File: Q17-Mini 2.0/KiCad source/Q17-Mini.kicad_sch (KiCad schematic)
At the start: 83 parts, among them J1 INPUT, J2-1 SPK+, J2-2 SPK-, J3-1 V+, J3-2 GND, J3-3 V-, Q1 IRF610, Q10 KSA992, Q12 KSC1845, Q13 IRF610, Q14 IRF9610, Q15 FQA46N15, Q16 IXTH48P20P, Q2 KSA992, Q3 KSC1845, Q4 IRF9610, Q5 FQPF7P20, Q6 2SK3564, Q7 LSK170B, Q8 DN2540, Q9 BS250P, U1 OPA1611, U2 NDC7003P

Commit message: Update BOM for Q17-Mini 2.0
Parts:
- R4: Mouser 594-MRS25000C1009FRP -> 594-MRS25000C1001FRP; Part# MRS25000C1009FRP00 -> MRS25000C1001FRP00
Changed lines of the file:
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@@
   (title_block
     (title "Q17-Mini Amplifier")
-    (date "2023-09-02")
+    (date "2023-09-14")
     (rev "2.0")
     (company "by eng. Tiberiu Vicol")
@@
       (effects (font (size 1.27 1.27)) hide)
     )
-    (property "Part#" "MRS25000C1009FRP00" (at 133.35 83.82 0)
-      (effects (font (size 1.27 1.27)) hide)
-    )
-    (property "Mouser" "594-MRS25000C1009FRP" (at 133.35 83.82 0)
-      (effects (font (size 1.27 1.27)) hide)
-    )
+    (property "Part#" "MRS25000C1001FRP00" (at 133.35 83.82 0)
+      (effects (font (size 1.27 1.27)) hide)
+    )
+    (property "Mouser" "594-MRS25000C1001FRP" (at 133.35 83.82 0)
+      (effects (font (size 1.27 1.27)) hide)
+    )

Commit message: Update schematic
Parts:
- R32: value STRAP -> 10R or STRAP; Mouser N.A -> 594-MRS25000C1009FRP; Part# N.A -> MRS25000C1009FRP00
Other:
- note added: "DC Offset at output < 1mV"
- note added: "DC Offset at output with R32 = 10R < 40mV"
- note added: "The value of R25 depends on the input voltage (42v = 2K7, 50v = 7K5, 60v = 8k2)."
- note removed: "DC Offset at output > 1mV"
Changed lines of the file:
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@@
   (title_block
     (title "Q17-Mini Amplifier")
-    (date "2023-09-14")
-    (rev "2.0")
+    (date "2023-09-24")
+    (rev "2.0.2")
     (company "by eng. Tiberiu Vicol")
     (comment 1 "Modified by Stef for the Q17-Mini project")
@@
   )
   (text "This will give you a coil of 10x20mm (see picture on github repository)."
-    (at 13.97 158.75 0)
+    (at 13.97 160.02 0)
     (effects (font (size 1.27 1.27) (thickness 0.254) bold) (justify left bottom))
   )
-  (text "For input sensibility at 1.5v: R17 = 7.32k" (at 177.8 160.02 0)
+  (text "For input sensibility at 1.5v: R17 = 7.32k" (at 177.8 157.48 0)
+    (effects (font (size 1.27 1.27)) (justify left bottom))
+  )
+  (text "The value of R25 depends on the input voltage (42v = 2K7, 50v = 7K5, 60v = 8k2)."
+    (at 177.8 162.56 0)
     (effects (font (size 1.27 1.27)) (justify left bottom))
   )
@@
   )
   (text "L1 : 19.5 turns of a 1mm diameter copper insulated wire wound around a 8mm tube."
-    (at 13.97 156.21 0)
+    (at 13.97 157.48 0)
     (effects (font (size 1.27 1.27) (thickness 0.254) bold) (justify left bottom))
   )
@@
     (effects (font (size 1.27 1.27)) (justify left bottom))
   )
-  (text "Transformer for 2 boards: 2 x 36Vac 160-250VA" (at 177.8 154.94 0)
+  (text "Transformer for 2 boards: 2 x 36Vac 160-250VA" (at 13.97 153.67 0)
     (effects (font (size 1.27 1.27) (thickness 0.254) bold) (justify left bottom))
   )
@@
     (effects (font (size 1.27 1.27)) (justify left bottom))
   )
-  (text "For input sensibility at 0.750v: R17 = 3.3k" (at 177.8 162.56 0)
+  (text "For input sensibility at 0.750v: R17 = 3.3k" (at 177.8 160.02 0)
     (effects (font (size 1.27 1.27)) (justify left bottom))
   )
@@
     (effects (font (size 1.27 1.27)) (justify left bottom))
   )
+  (text "DC Offset at output with R32 = 10R < 40mV" (at 13.97 30.48 0)
+    (effects (font (size 1.27 1.27)) (justify left bottom))
+  )
   (text "C17 : 100nF capacitor FKP3C031004C00JSSD or MKT1822410255."
     (at 107.95 189.23 0)
@@
     (effects (font (size 1.27 1.27)) (justify left bottom))
   )
-  (text "DC Offset at output > 1mV" (at 13.97 27.94 0)
+  (text "DC Offset at output < 1mV" (at 13.97 27.94 0)
     (effects (font (size 1.27 1.27)) (justify left bottom))
   )
@@
       (effects (font (size 1.27 1.27)) (justify left))
     )
-    (property "Value" "STRAP" (at 270.9647 146.2422 90)
+    (property "Value" "10R or STRAP" (at 274.32 146.05 90)
       (effects (font (size 1.27 1.27)) (justify left))
     )
@@
       (effects (font (size 1.27 1.27)) hide)
     )
-    (property "Datasheet" "~" (at 267.97 148.59 0)
+    (property "Datasheet" "https://www.vishay.com/doc?28724" (at 267.97 148.59 0)
       (effects (font (size 1.27 1.27)) hide)
     )
-    (property "Part#" "N.A" (at 267.97 148.59 90)
+    (property "Part#" "MRS25000C1009FRP00" (at 267.97 148.59 90)
       (effects (font (size 1.27 1.27)) hide)
     )
-    (property "Mouser" "N.A" (at 267.97 148.59 90)
+    (property "Mouser" "594-MRS25000C1009FRP" (at 267.97 148.59 90)
       (effects (font (size 1.27 1.27)) hide)
     )

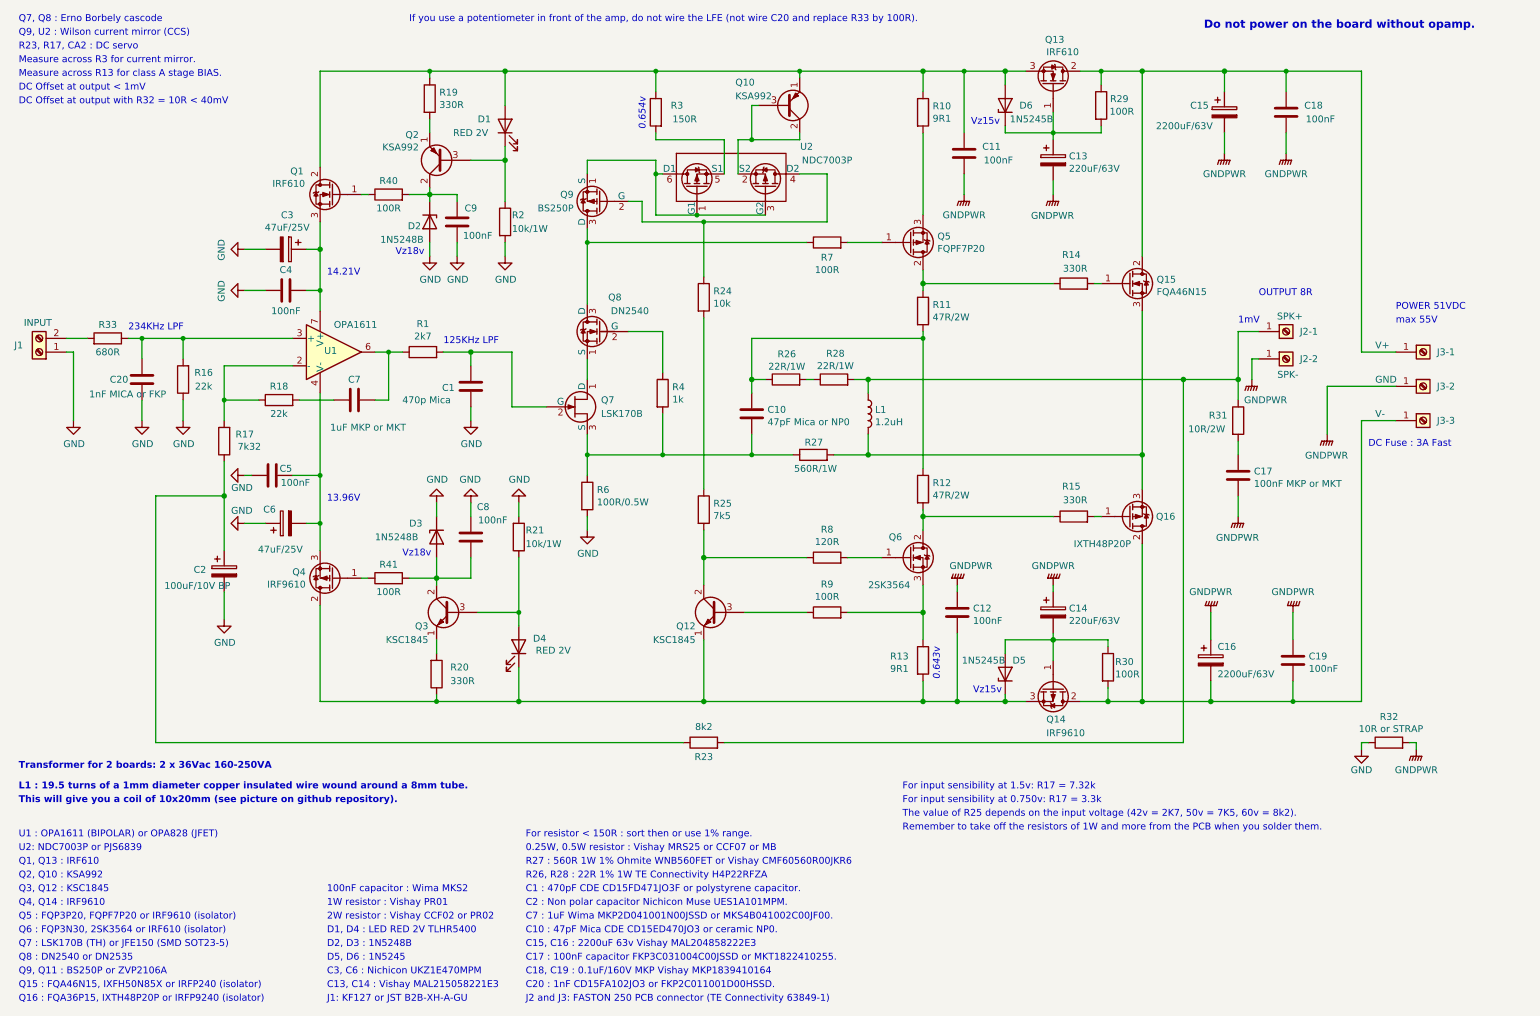
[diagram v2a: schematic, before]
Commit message: Q17-Mini-schematic 2.0.3 with measures
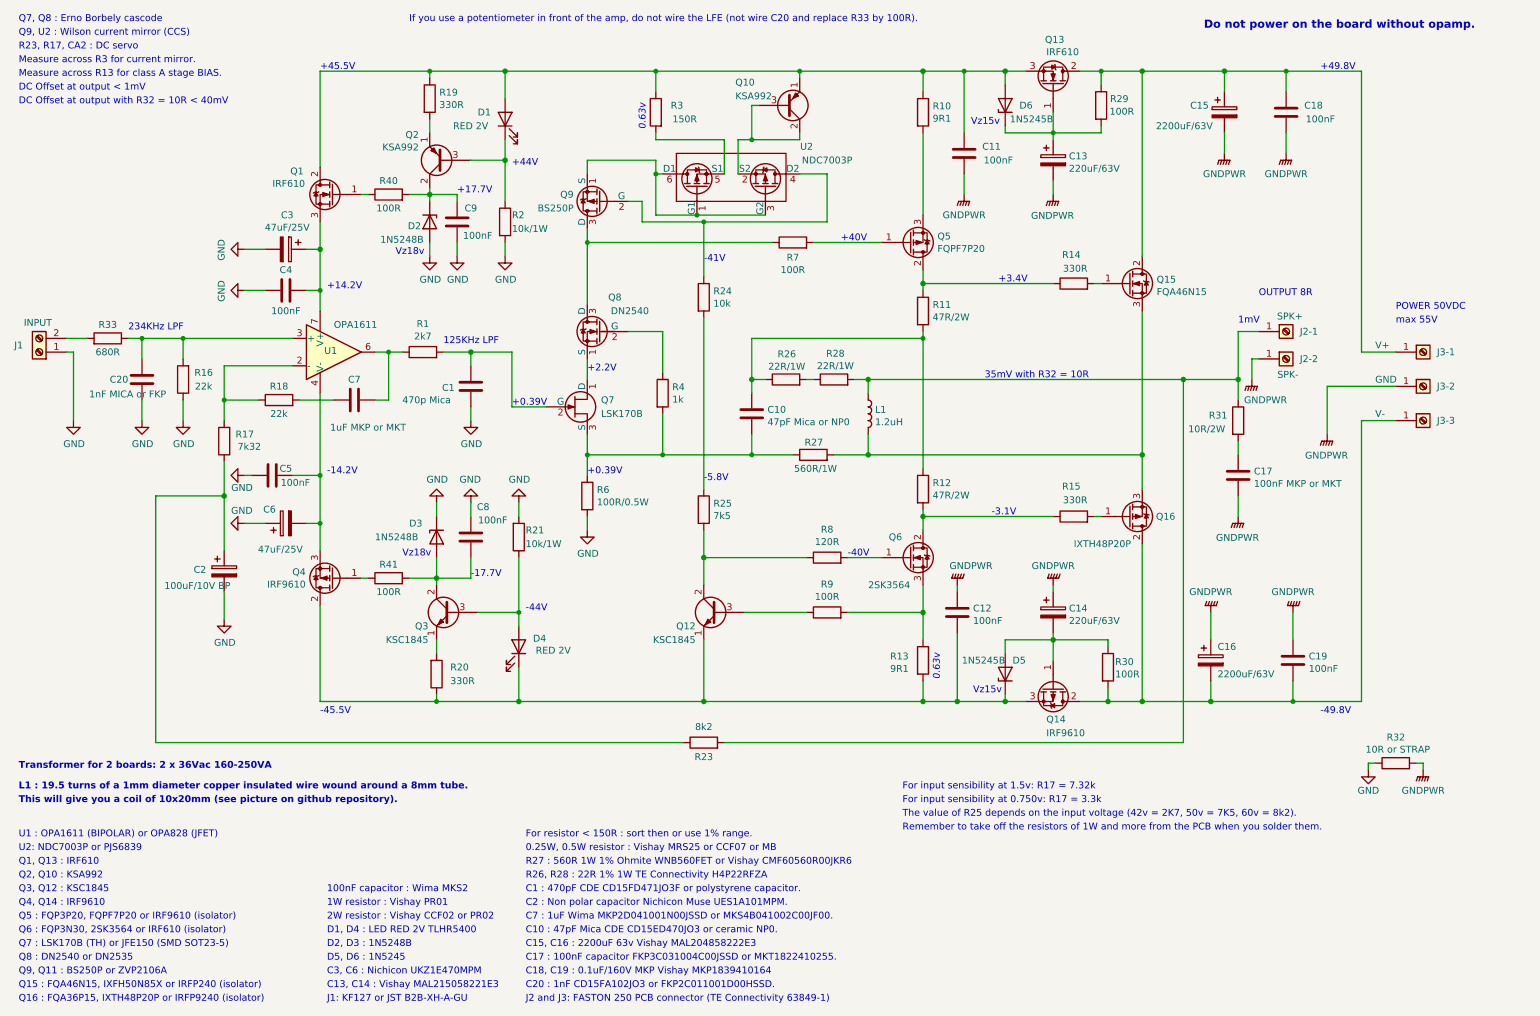
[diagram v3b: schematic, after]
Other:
- note added: "+0.39V"
- note added: "+14.2V"
- note added: "+17.7V"
- note added: "+2.2V"
- note added: "+3.4V"
- note added: "+40V"
- note added: "+44V"
- note added: "+45.5V"
- note added: "+49.8V"
- note added: "-14.2V"
- note added: "-17.7V"
- note added: "-3.1V"
- note added: "-40V"
- note added: "-41V"
- note added: "-44V"
- note added: "-45.5V"
- note added: "-49.8V"
- note added: "-5.8V"
- note added: "0.63v"
- note added: "35mV with R32 = 10R"
- note added: "POWER 50VDC"
- note removed: "0.643v"
- note removed: "0.654v"
- note removed: "13.96V"
- note removed: "14.21V"
- note removed: "DC Fuse : 3A Fast"
- note removed: "POWER 51VDC"
- title: Q17-Mini Amplifier -> Q17-Mini Amplifier 2.x
- moved on the sheet: D1, R32, R7

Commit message: Update Q17-Mini-schematic 2.0.4
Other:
- note added: "Transformer for 2 boards: 2 x 37Vac 160-250VA"
- note removed: "Transformer for 2 boards: 2 x 36Vac 160-250VA"
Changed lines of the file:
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@@
   (title_block
     (title "Q17-Mini Amplifier 2.x")
-    (date "2024-01-06")
-    (rev "2.0.3")
+    (date "2024-01-11")
+    (rev "2.0.4")
     (company "by eng. Tiberiu Vicol")
     (comment 1 "Modified by Stef for the Q17-Mini project")
@@
     (effects (font (size 1.27 1.27)) (justify left bottom))
   )
-  (text "Transformer for 2 boards: 2 x 36Vac 160-250VA" (at 13.97 153.67 0)
+  (text "Transformer for 2 boards: 2 x 37Vac 160-250VA" (at 13.97 153.67 0)
     (effects (font (size 1.27 1.27) (thickness 0.254) bold) (justify left bottom))
   )

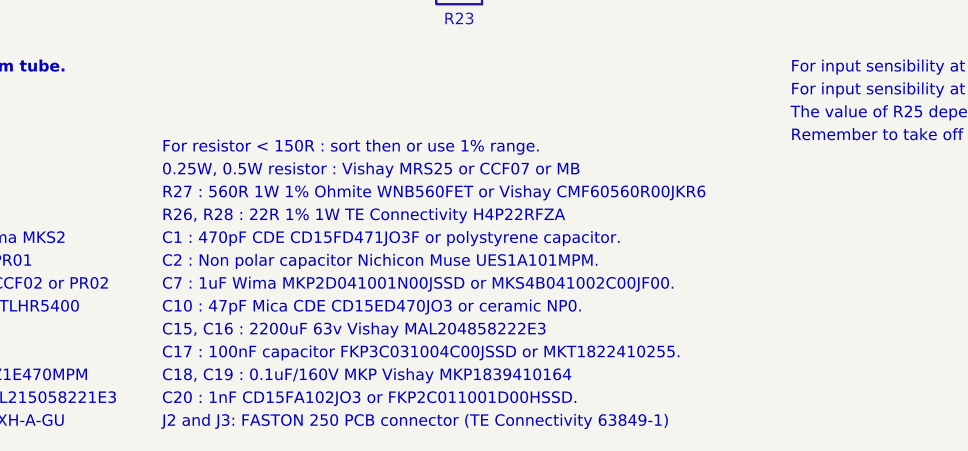
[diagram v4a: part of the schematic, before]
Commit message: Update Q17-Mini diagram (C7 parts)
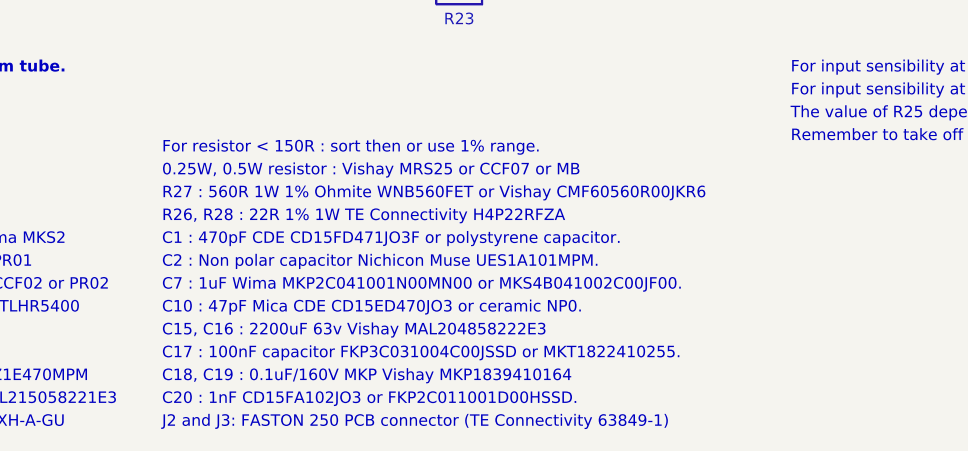
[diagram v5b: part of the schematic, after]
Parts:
- C7: Mouser https://www.ebay.fr/itm/164258731098 -> 505-MKP2C0411NMN; Part# MKP2D041001N00JSSD -> MKP2C041001N00MN00
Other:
- note added: "C7 : 1uF Wima MKP2C041001N00MN00 or MKS4B041002C00JF00."
- note removed: "C7 : 1uF Wima MKP2D041001N00JSSD or MKS4B041002C00JF00."
